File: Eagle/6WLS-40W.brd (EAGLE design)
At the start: 409.3 x 131.1 mm, 36 parts, among them J1 12VDC-8A, SW1 SPDTTHRU, U1 DCDCEC7C01, U2 DCDCEC7C03, U3 DCDCEC7C03

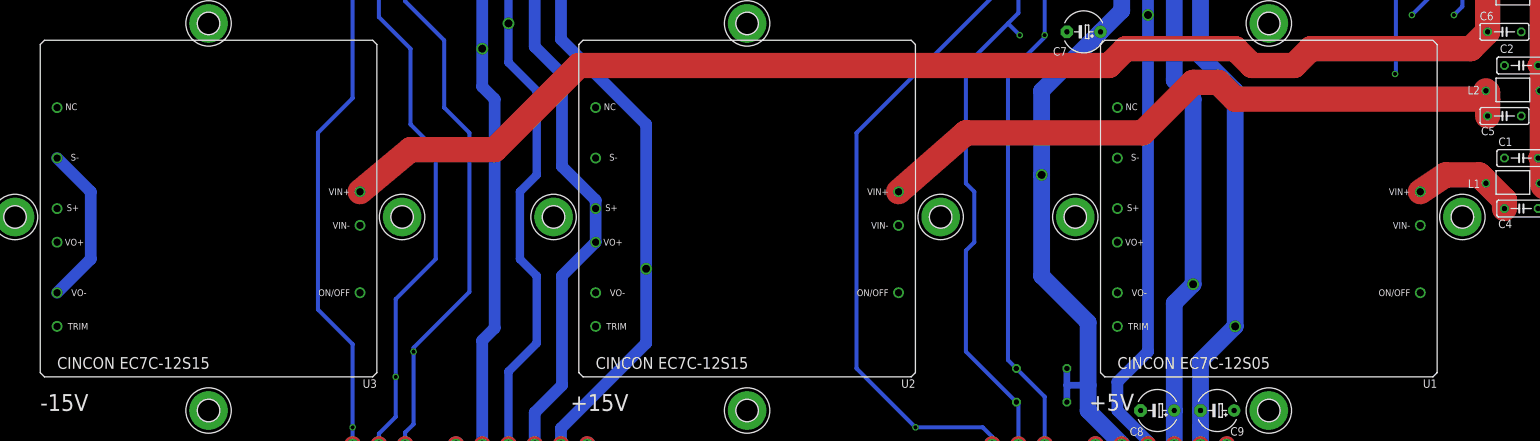
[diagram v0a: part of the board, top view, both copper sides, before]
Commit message: Move supplies down to clear upper mounting screws.
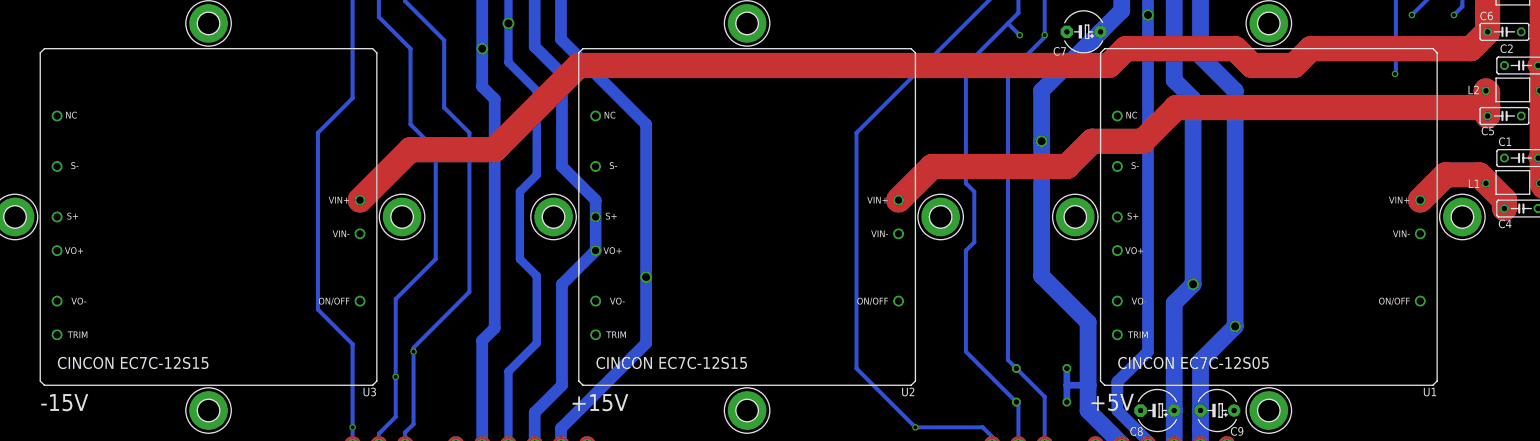
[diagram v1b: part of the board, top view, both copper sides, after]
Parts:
- moved U1 1.27 mm to (355.6, 34.3)
- moved U2 1.27 mm to (276.9, 34.3)
- moved U3 1.27 mm to (195.6, 34.3)
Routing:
- net 15V+: track 757.7 -> 767.4 mm
- net 5V+: track 918.6 -> 922.4 mm
- net 15V-: track 759.2 -> 762.5 mm
- net GND: track 52.1 -> 49.5 mm
- net N$1: track 100.4 -> 98.6 mm
- net N$2: track 187.8 -> 188.6 mm
- net N$3: track 17.1 -> 17.9 mm
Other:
- board text added: "6WLS-40W R2 3/23 DC (WITH THANKS TO D. BROWN)"
- board text removed: "6WLS-40W R1 6/22 DC (WITH THANKS TO D. BROWN)"

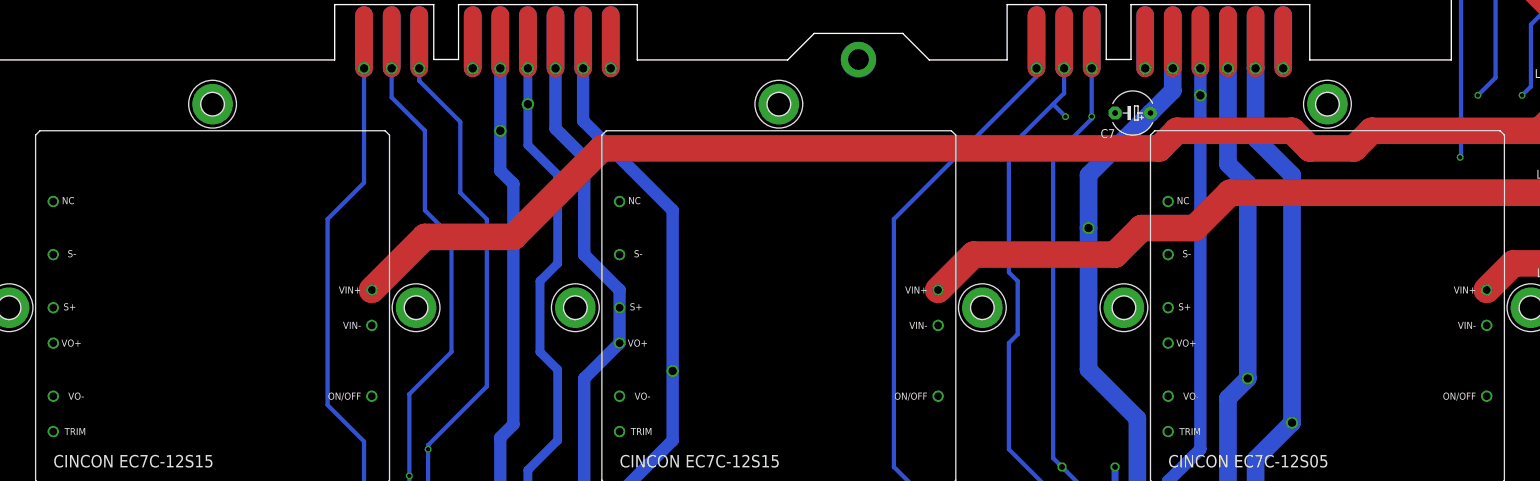
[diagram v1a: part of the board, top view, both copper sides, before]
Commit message: Larger copper pads for supply pins.
Switch to larger, oblong pads for supply pins. Thanks to Prism Circuits.
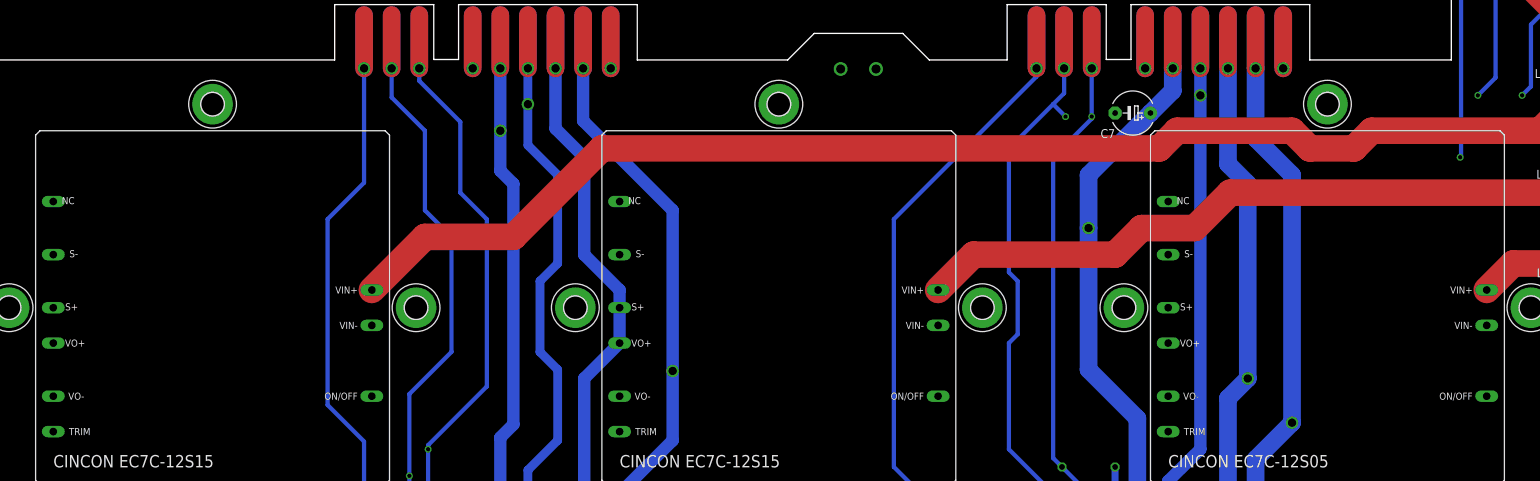
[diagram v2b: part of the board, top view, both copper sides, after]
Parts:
- added X1: MKDSN1,5/2-5,08, con-phoenix-508:MKDSN1,5/2-5,08
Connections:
- net GND: now also X1.1, X1.2
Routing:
- net GND: track 49.5 -> 54.5 mm
- net QGND: vias 9 -> 8
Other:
- board text added: "6WLS-40W R3 11/24 DC (WITH THANKS TO D. BROWN)"
- board text removed: "6WLS-40W R2 3/23 DC (WITH THANKS TO D. BROWN)"
- board text removed: "BANANA"
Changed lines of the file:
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@@
 <plain>
 <text x="161.544" y="32.3469" size="6.096" layer="26" font="vector" ratio="12" rot="MR0">STUDIOHSOFTWARE.COM</text>
-<text x="147.574" y="29.1465" size="1.778" layer="26" font="vector" ratio="12" rot="MR0">6WLS-40W R2 3/23 DC (WITH THANKS TO D. BROWN)</text>
+<text x="147.574" y="29.1465" size="1.778" layer="26" font="vector" ratio="12" rot="MR0">6WLS-40W R3 11/24 DC (WITH THANKS TO D. BROWN)</text>
 <wire x1="66.04" y1="0" x2="66.04" y2="-7.9375" width="0.0254" layer="20"/>
 <wire x1="66.04" y1="-7.9375" x2="40.386" y2="-7.9375" width="0.0254" layer="20"/>
@@
 <wire x1="401.32" y1="0" x2="353.06" y2="0" width="0.0254" layer="20"/>
 <text x="326.6186" y="14.6939" size="1.27" layer="26" font="vector" ratio="12" rot="MR0">I2C PULLUPS </text>
-<text x="285.4198" y="71.3359" size="1.27" layer="26" font="vector" ratio="12" rot="MR0">GND</text>
-<text x="285.4198" y="69.6595" size="1.27" layer="26" font="vector" ratio="12" rot="MR0">BANANA</text>
 <wire x1="401.32" y1="123.19" x2="401.32" y2="101.6" width="0.0254" layer="20"/>
 <wire x1="401.32" y1="101.6" x2="393.7" y2="93.98" width="0.0254" layer="20"/>
@@
 <text x="254" y="12.6365" size="1.778" layer="25" font="vector" ratio="12">CINCON EC7C-12S15</text>
 <text x="172.72" y="12.6365" size="1.778" layer="25" font="vector" ratio="12">CINCON EC7C-12S15</text>
+<text x="287.3502" y="64.262" size="1.27" layer="26" font="vector" ratio="12" rot="MR0">GND</text>
+<text x="292.4302" y="64.262" size="1.27" layer="26" font="vector" ratio="12" rot="MR0">GND</text>
 </plain>
 <attributes>
@@
 <attribute name="VALUE" x="322.8848" y="115.316" size="1.27" layer="27" font="vector" ratio="12" rot="R90"/>
 </element>
+<element name="X1" library="con-phoenix-508" package="MKDSN1,5/2-5,08" value="MKDSN1,5/2-5,08" x="288.29" y="69.85" smashed="yes" rot="MR180"/>
 </elements>
 <signals>
@@
 <via x="349.25" y="69.914771875" extent="1-16" drill="1.2"/>
 <wire x1="349.25" y1="69.914771875" x2="349.25" y2="77.566521875" width="2.54" layer="16"/>
-<via x="288.29" y="71.184771875" extent="1-16" drill="2.95" diameter="5.08"/>
 <contactref element="C8" pad="-"/>
 <contactref element="C9" pad="+"/>
 <contactref element="U3" pad="VO+"/>
-<wire x1="288.29" y1="71.184771875" x2="288.29" y2="71.12" width="5.08" layer="16"/>
 <contactref element="U2" pad="VO-"/>
 <contactref element="U2" pad="S-"/>
@@
 <wire x1="254" y1="43.18" x2="254" y2="22.86" width="0" layer="19" extent="1-1"/>
 <wire x1="252.73" y1="69.914771875" x2="254" y2="43.18" width="0" layer="19" extent="1-1"/>
-<wire x1="288.29" y1="71.184771875" x2="252.73" y2="69.914771875" width="0" layer="19" extent="1-1"/>
-<wire x1="349.25" y1="69.914771875" x2="288.29" y2="71.184771875" width="0" layer="19" extent="1-1"/>
-<wire x1="350.3676" y1="6.35" x2="349.25" y2="69.914771875" width="0" layer="19" extent="1-1"/>
-<wire x1="349.25" y1="1.2065" x2="350.3676" y2="6.35" width="0" layer="19" extent="16-16"/>
-<wire x1="336.2452" y1="6.35" x2="349.25" y2="1.2065" width="0" layer="19" extent="16-16"/>
 <wire x1="172.72" y1="35.56" x2="254" y2="43.18" width="0" layer="19" extent="1-1"/>
 <wire x1="172.72" y1="30.48" x2="172.72" y2="35.56" width="0" layer="19" extent="1-1"/>
 <wire x1="161.29" y1="1.2065" x2="172.72" y2="30.48" width="0" layer="19" extent="16-16"/>
+<wire x1="336.2452" y1="6.35" x2="252.73" y2="1.2065" width="0" layer="19" extent="16-16"/>
+<wire x1="349.25" y1="1.2065" x2="336.2452" y2="6.35" width="0" layer="19" extent="16-16"/>
+<wire x1="350.3676" y1="6.35" x2="349.25" y2="1.2065" width="0" layer="19" extent="16-16"/>
+<wire x1="349.25" y1="69.914771875" x2="350.3676" y2="6.35" width="0" layer="19" extent="1-1"/>
 <wire x1="62.23" y1="-6.4135" x2="161.29" y2="-6.4135" width="0" layer="19" extent="16-16"/>
 <wire x1="62.23" y1="69.914771875" x2="62.23" y2="1.2065" width="0" layer="19" extent="1-16"/>
@@
 <wire x1="337.3628" y1="66.04" x2="337.3628" y2="69.914771875" width="1.778" layer="16"/>
 <wire x1="350.52" y1="66.04" x2="337.3628" y2="66.04" width="1.778" layer="15"/>
-<wire x1="337.3628" y1="66.04" x2="285.75" y2="66.04" width="1.778" layer="15"/>
-<wire x1="265.8618" y1="69.0118" x2="282.7782" y2="69.0118" width="1.778" layer="15"/>
-<wire x1="282.7782" y1="69.0118" x2="285.75" y2="66.04" width="1.778" layer="15"/>
+<wire x1="337.3628" y1="66.04" x2="283.21" y2="66.04" width="1.778" layer="15"/>
+<wire x1="265.8618" y1="69.0118" x2="280.2382" y2="69.0118" width="1.778" layer="15"/>
+<wire x1="280.2382" y1="69.0118" x2="283.21" y2="66.04" width="1.778" layer="15"/>
 <wire x1="265.8618" y1="69.0118" x2="262.89" y2="66.04" width="1.778" layer="15"/>
 <wire x1="262.89" y1="66.04" x2="246.38" y2="66.04" width="1.778" layer="15"/>
@@
 <wire x1="329.438" y1="69.85" x2="329.4634" y2="69.85" width="2.54" layer="2"/>
 <wire x1="349.2754" y1="69.8754" x2="349.3008" y2="69.8754" width="2.54" layer="2"/>
-<wire x1="289.56" y1="71.12" x2="287.02" y2="71.12" width="5.08" layer="2"/>
 <wire x1="389.001" y1="117.221" x2="390.779" y2="117.221" width="3.81" layer="2"/>
 <wire x1="350.3422" y1="6.2738" x2="350.3168" y2="6.2738" width="2.54" layer="2"/>
@@
 <wire x1="252.73" y1="43.18" x2="254" y2="43.18" width="2.54" layer="2"/>
 <wire x1="172.72" y1="30.48" x2="173.99" y2="30.48" width="2.54" layer="2"/>
+<contactref element="X1" pad="1"/>
+<contactref element="X1" pad="2"/>
+<wire x1="292.1" y1="69.85" x2="284.48" y2="69.85" width="5.08" layer="2"/>
 <wire x1="232.918" y1="1.1938" x2="252.7046" y2="1.1938" width="0" layer="19" extent="2-2"/>
 <wire x1="252.73" y1="22.86" x2="252.7046" y2="1.1938" width="0" layer="19" extent="2-2"/>
@@
 <wire x1="252.73" y1="69.9262" x2="252.73" y2="43.18" width="0" layer="19" extent="2-2"/>
 <wire x1="232.9434" y1="69.9262" x2="252.73" y2="69.9262" width="0" layer="19" extent="2-2"/>
-<wire x1="161.29" y1="1.27" x2="172.72" y2="30.48" width="0" layer="19" extent="2-2"/>
+<wire x1="161.3154" y1="1.27" x2="172.72" y2="30.48" width="0" layer="19" extent="2-2"/>
 <wire x1="141.478" y1="1.1684" x2="161.29" y2="1.27" width="0" layer="19" extent="2-2"/>
-<wire x1="287.02" y1="71.12" x2="252.7554" y2="69.9262" width="0" layer="19" extent="2-2"/>
 <wire x1="62.23" y1="1.2192" x2="141.4526" y2="1.1684" width="0" layer="19" extent="2-2"/>
 <wire x1="42.418" y1="1.2446" x2="62.2046" y2="1.2192" width="0" layer="19" extent="2-2"/>
